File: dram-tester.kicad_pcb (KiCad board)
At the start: 2 copper layers, 53.3 x 52.1 mm, 9 parts, among them J1 Zif Socket, SW1 Reset

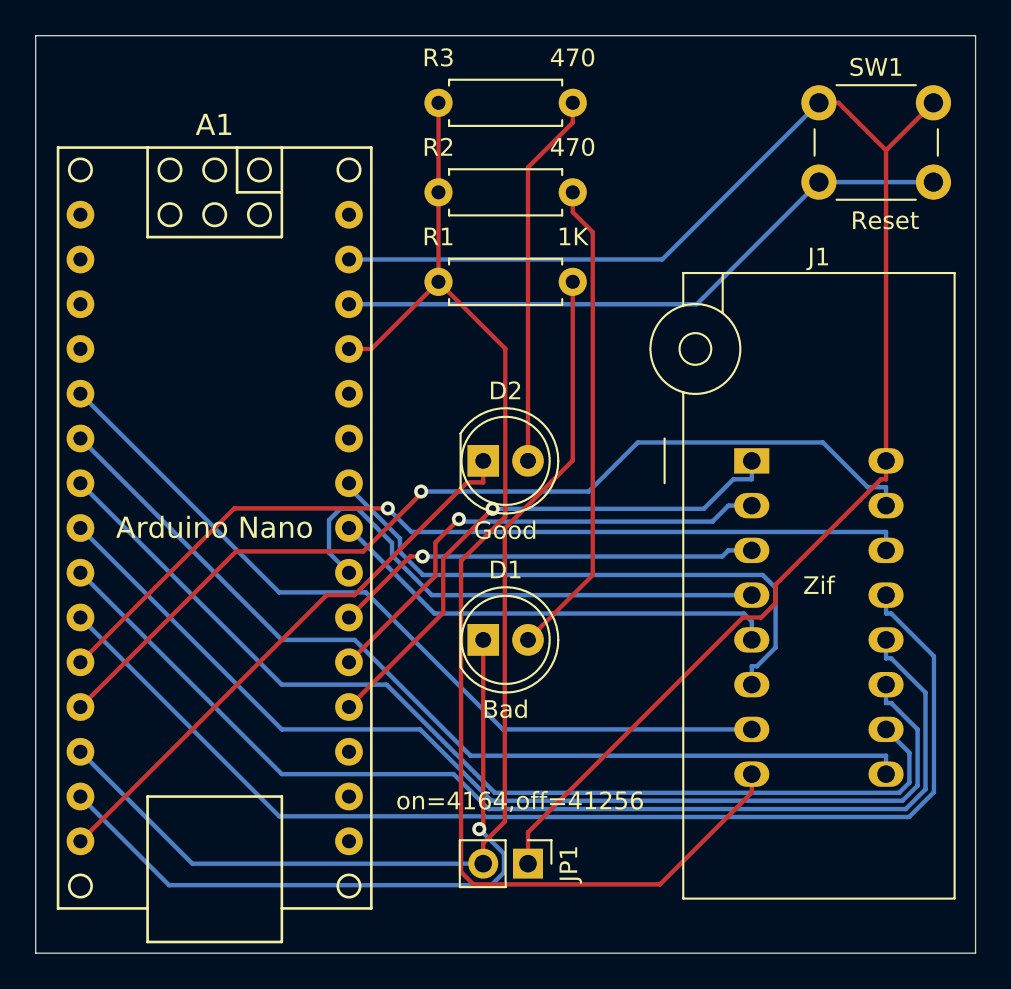
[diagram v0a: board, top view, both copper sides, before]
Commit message: added ground plane
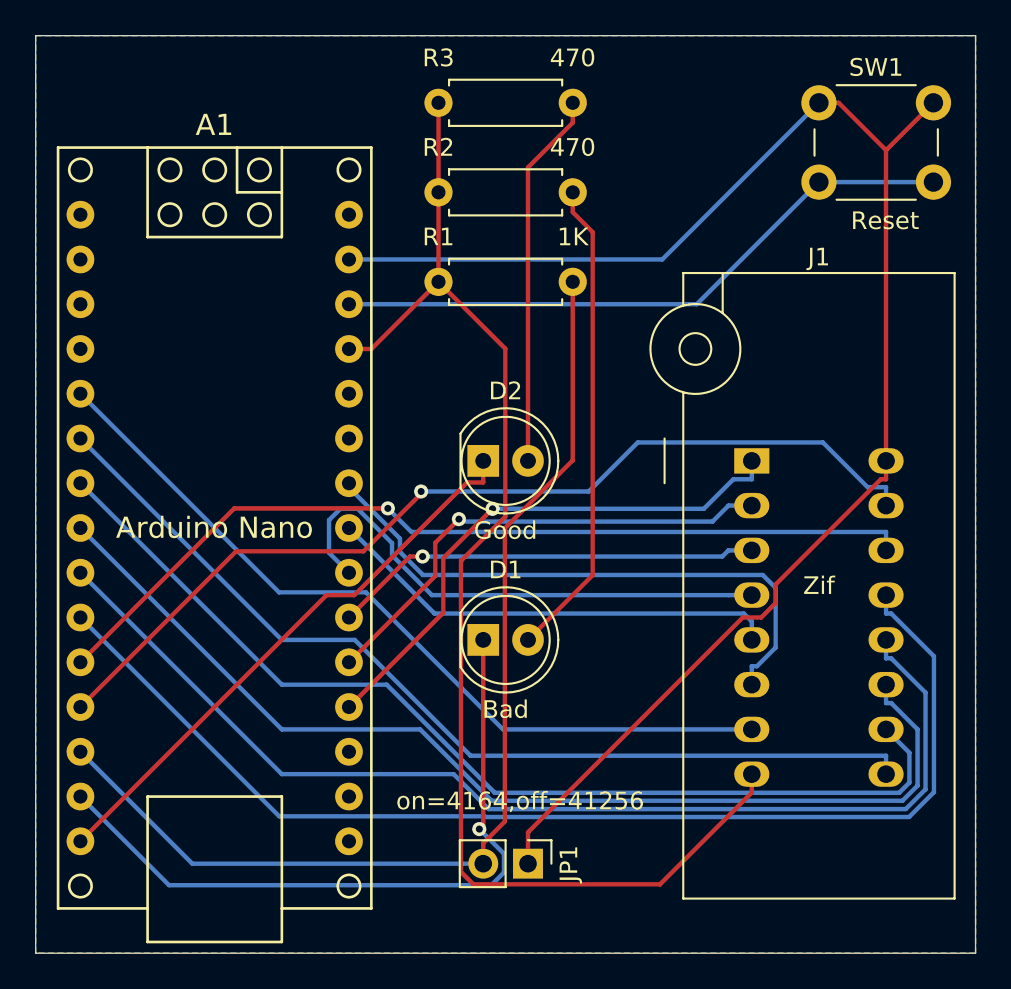
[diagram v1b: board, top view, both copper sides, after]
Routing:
- added copper zone on B.Cu, net Net-(A1-Pad29)
- added copper zone on F.Cu, net Net-(A1-Pad29)

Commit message: cleaned up pcb
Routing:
- net Net-(A1-Pad14): track 40.3 -> 51.2 mm
- net Net-(A1-Pad12): track 54.1 -> 57.8 mm
- net Net-(A1-Pad22): track 30.2 -> 33.2 mm
- net Net-(A1-Pad23): track 26.1 -> 28.3 mm
- net Net-(A1-Pad11): track 50.9 -> 53.0 mm
- net Net-(A1-Pad19): track 31.1 -> 29.4 mm
- net Net-(A1-Pad24): track 33.5 -> 35.0 mm
- net Net-(A1-Pad29): track 88.8 -> 90.1 mm
- net Net-(A1-Pad6): track 54.2 -> 53.0 mm
- net Net-(A1-Pad27): track 72.9 -> 71.8 mm
- net Net-(A1-Pad8): track 60.9 -> 60.1 mm
- net Net-(A1-Pad9): track 63.6 -> 62.8 mm
- net Net-(A1-Pad13): track 60.6 -> 59.9 mm
- net Net-(A1-Pad10): track 66.2 -> 65.6 mm
- net Net-(A1-Pad7): track 58.1 -> 57.6 mm
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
